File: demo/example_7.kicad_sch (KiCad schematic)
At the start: 6 parts, among them U7 LDO

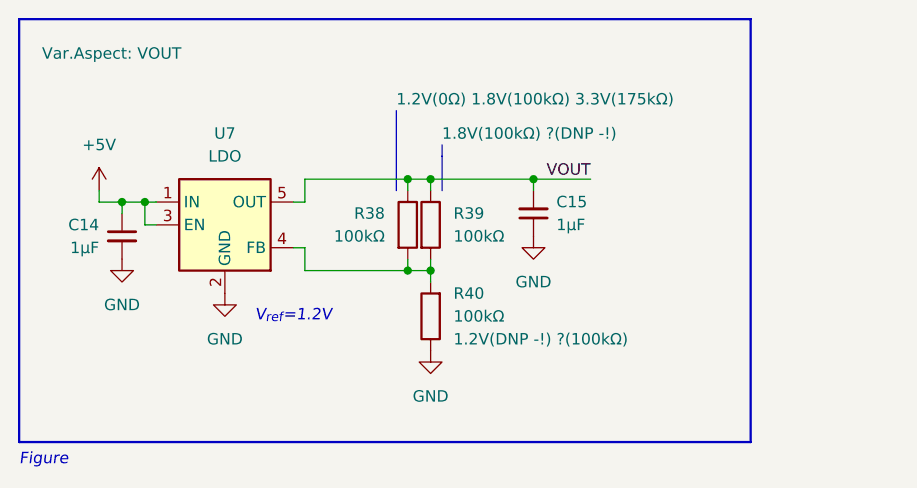
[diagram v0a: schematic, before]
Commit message: Example 7: Also switch solder paste
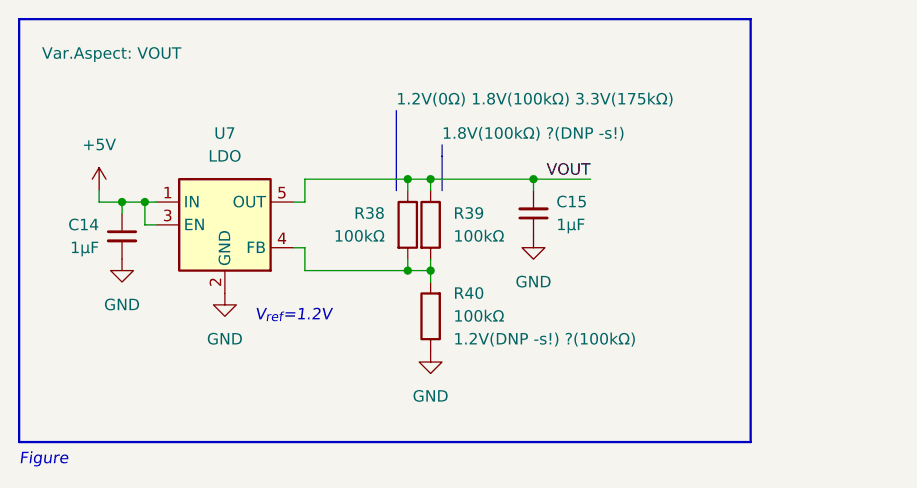
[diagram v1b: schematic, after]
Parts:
- R39: Var 1.8V(100kΩ) ?(DNP -!) -> 1.8V(100kΩ) ?(DNP -s!)
- R40: Var 1.2V(DNP -!) ?(100kΩ) -> 1.2V(DNP -s!) ?(100kΩ)
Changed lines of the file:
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@@
 			)
 		)
-		(property "Var" "1.2V(DNP -!) ?(100kΩ)"
+		(property "Var" "1.2V(DNP -s!) ?(100kΩ)"
 			(at 109.22 69.8499 0)
 			(effects
@@
 			)
 		)
-		(property "Var" "1.8V(100kΩ) ?(DNP -!)"
+		(property "Var" "1.8V(100kΩ) ?(DNP -s!)"
 			(at 107.95 46.99 0)
 			(do_not_autoplace yes)

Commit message: Example 7: Add 2.5V choice, refine
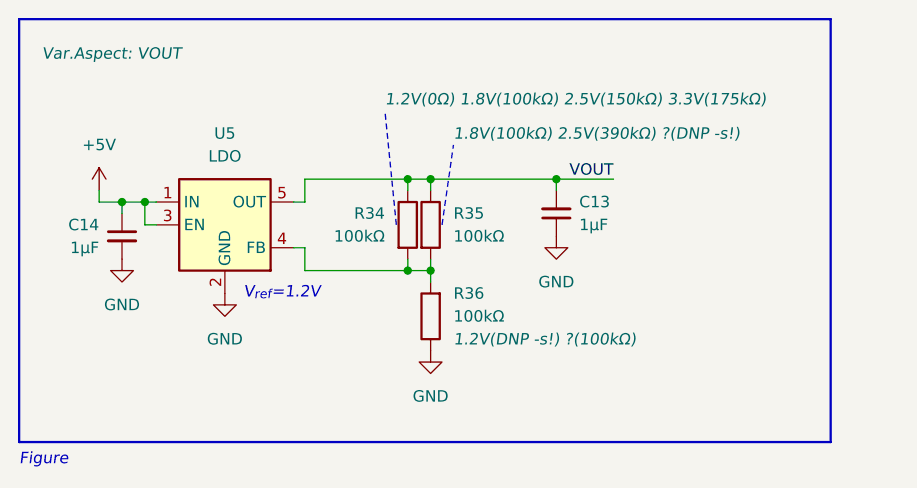
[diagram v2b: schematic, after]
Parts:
- removed C15: 1µF, Capacitor_SMD:C_0603_1608Metric, symbol Device:C_Small
- removed R38, R39, R40: 100kΩ, Resistor_SMD:R_0402_1005Metric_Pad0.72x0.64mm_HandSolder, symbol Device:R
- removed U7: LDO, Package_TO_SOT_SMD:SOT-23-5, symbol Regulator_Linear:TLV75801PDBV
- added C13: 1µF, Capacitor_SMD:C_0603_1608Metric, symbol Device:C_Small
- added R34, R35, R36: 100kΩ, Resistor_SMD:R_0402_1005Metric_Pad0.72x0.64mm_HandSolder, symbol Device:R
- added U5: LDO, Package_TO_SOT_SMD:SOT-23-5, symbol Regulator_Linear:TLV75801PDBV
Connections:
- net +5V: now also U5.1 (IN), U5.3 (EN)
- net GND: now also C13.1, R36.1, U5.2 (GND)
- net VOUT: now also C13.2, R34.1, R35.1, U5.5 (OUT)
- new net: R34.2, R35.2, R36.2, U5.4 (FB)
